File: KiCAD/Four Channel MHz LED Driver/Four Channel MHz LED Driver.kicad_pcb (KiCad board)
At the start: 2 copper layers, 100 x 100 mm, 92 parts, among them J1 Barrel_Jack_Switch, J10 Conn_01x24_Female, J2 Conn_01x02_Female, J3 8P8C_Shielded_x4, J4 Conn_01x03_Male, J5 Conn_01x03_Female, J6 Conn_01x08_Female, J7 Conn_01x03_Female, J8 Conn_01x05_Female, J9 Conn_01x24_Female, M1 Fan_4pin, Q1 SUM70060E, SW1 Pushbutton_with_LED, SW2 Pushbutton_with_LED, SW3 Pushbutton_with_LED, SW4 Pushbutton_with_LED, SW5 SW_SPDT, U1 12V boost, U10 ASSR-1218, U11 ASSR-1218, U12 Teensy3.6, U2 SN74LV4T125PWR, U3 DPBW06F-05, U4 TMUX1204DGSR, U5 BDJ0GA5WEFJ-E2, U6 ADP7182AUJZ-1.8-R7, U7 LT6200CS8-10, U8 ASSR-1218, U9 ASSR-1218

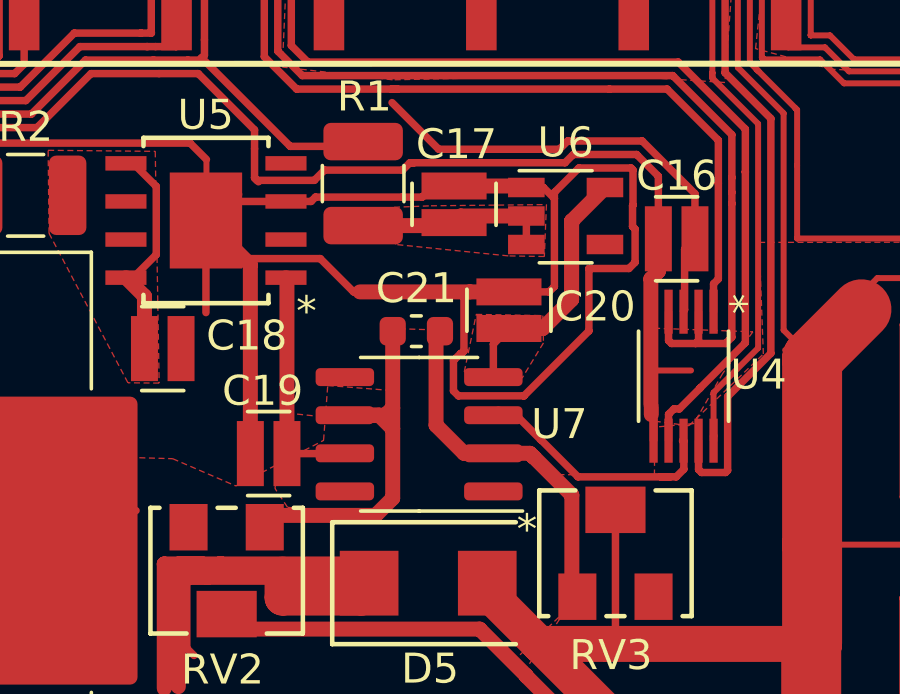
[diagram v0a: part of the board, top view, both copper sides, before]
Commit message: better LDO output bypass
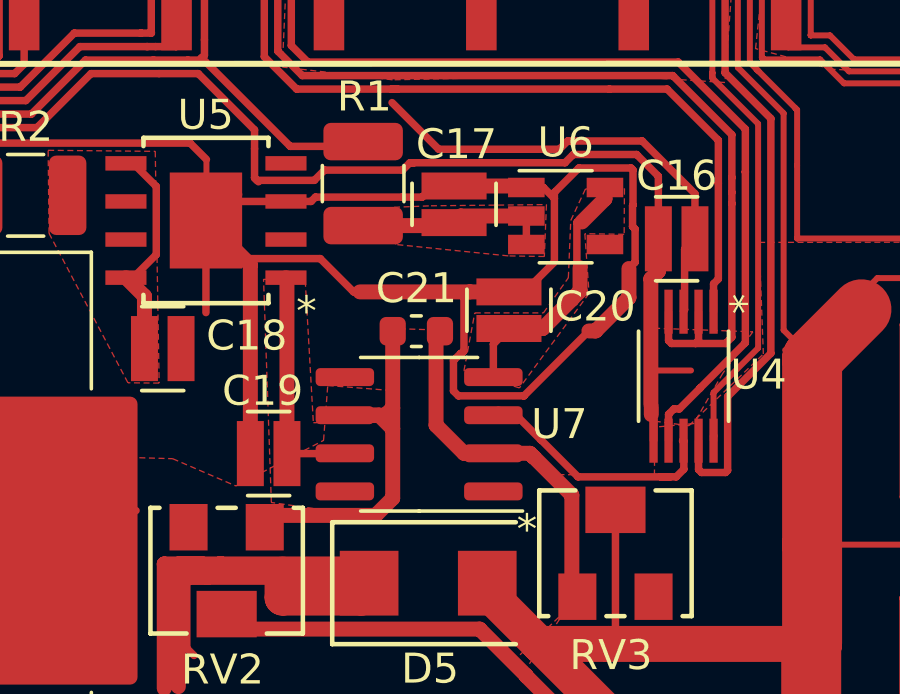
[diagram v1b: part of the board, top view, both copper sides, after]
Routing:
- net /-1.8V-analog: track 12.6 -> 8.70 mm
- net GND: track 1125.0 -> 1123.9 mm
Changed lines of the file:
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@@
     (thickness 1.6)
     (drawings 18)
-    (tracks 1936)
+    (tracks 1940)
     (zones 0)
     (modules 92)
@@
   (segment (start 59.11 58.57) (end 64.46 58.57) (width 0.25) (layer F.Cu) (net 2))
   (segment (start 82.77221 78.48) (end 78.81 78.48) (width 0.25) (layer F.Cu) (net 2))
-  (segment (start 96.885 71.19) (end 95.55 71.19) (width 0.25) (layer F.Cu) (net 2))
-  (segment (start 97.065001 71.009999) (end 96.885 71.19) (width 0.25) (layer F.Cu) (net 2))
-  (segment (start 97.065001 68.074999) (end 97.065001 71.009999) (width 0.25) (layer F.Cu) (net 2))
   (segment (start 96.700002 67.71) (end 97.065001 68.074999) (width 0.25) (layer F.Cu) (net 2))
   (segment (start 96.13 67.71) (end 96.700002 67.71) (width 0.25) (layer F.Cu) (net 2))
@@
   (segment (start 45.82 49.52) (end 46.66 50.36) (width 0.5) (layer F.Cu) (net 2))
   (segment (start 41.44 49.52) (end 45.82 49.52) (width 0.5) (layer F.Cu) (net 2))
-  (segment (start 98.215021 72.491747) (end 98.215021 70.41) (width 0.25) (layer F.Cu) (net 2))
   (segment (start 96.051758 74.65501) (end 98.215021 72.491747) (width 0.25) (layer F.Cu) (net 2))
   (segment (start 99.754999 69.094997) (end 99.67 69.009998) (width 0.25) (layer F.Cu) (net 2))
   (segment (start 99.754999 70.205001) (end 99.754999 69.094997) (width 0.25) (layer F.Cu) (net 2))
-  (segment (start 98.215021 70.41) (end 99.55 70.41) (width 0.25) (layer F.Cu) (net 2))
   (segment (start 99.55 70.41) (end 99.754999 70.205001) (width 0.25) (layer F.Cu) (net 2))
   (segment (start 62.27 103.77) (end 60.34 105.7) (width 2) (layer F.Cu) (net 2))
@@
   (segment (start 76.31998 66.23002) (end 84.92222 66.23002) (width 0.25) (layer F.Cu) (net 2))
   (segment (start 74.87 66.23002) (end 76.31998 66.23002) (width 0.25) (layer F.Cu) (net 2))
+  (segment (start 98.215021 72.491747) (end 98.438253 72.491747) (width 0.5) (layer F.Cu) (net 2))
+  (segment (start 99.55 71.38) (end 99.55 70.41) (width 0.5) (layer F.Cu) (net 2))
+  (segment (start 98.438253 72.491747) (end 99.55 71.38) (width 0.5) (layer F.Cu) (net 2))
+  (segment (start 96.070002 71.19) (end 95.55 71.19) (width 0.25) (layer F.Cu) (net 2))
+  (segment (start 97.065001 70.195001) (end 96.070002 71.19) (width 0.25) (layer F.Cu) (net 2))
+  (segment (start 97.065001 68.074999) (end 97.065001 70.195001) (width 0.25) (layer F.Cu) (net 2))
   (segment (start 45.34 54.5) (end 43.92 53.08) (width 0.25) (layer F.Cu) (net 3))
   (segment (start 45.34 56.08) (end 45.34 54.5) (width 0.25) (layer F.Cu) (net 3))
@@
   (segment (start 88.15 70.748) (end 88.117 70.715) (width 0.5) (layer F.Cu) (net 8))
   (segment (start 88.15 76.58) (end 88.15 70.748) (width 0.5) (layer F.Cu) (net 8))
-  (segment (start 98.75 67.71) (end 97.515011 68.944989) (width 0.25) (layer F.Cu) (net 9))
-  (segment (start 97.515011 68.944989) (end 97.51501 71.1964) (width 0.25) (layer F.Cu) (net 9))
   (segment (start 95.03 72.93) (end 95.55 72.41) (width 0.25) (layer F.Cu) (net 9))
   (segment (start 95.03 74.03) (end 95.03 72.93) (width 0.25) (layer F.Cu) (net 9))
-  (segment (start 97.640011 68.830011) (end 97.640011 68.944989) (width 0.5) (layer F.Cu) (net 9))
   (segment (start 98.75 67.71) (end 98.75 67.720022) (width 0.5) (layer F.Cu) (net 9))
-  (segment (start 98.75 67.720022) (end 97.640011 68.830011) (width 0.5) (layer F.Cu) (net 9))
-  (segment (start 97.640011 68.830011) (end 97.640011 71.248175) (width 0.5) (layer F.Cu) (net 9))
-  (segment (start 97.640011 71.444991) (end 97.640011 71.248175) (width 0.5) (layer F.Cu) (net 9))
   (segment (start 95.55 72.41) (end 96.675002 72.41) (width 0.5) (layer F.Cu) (net 9))
   (segment (start 96.675002 72.41) (end 97.640011 71.444991) (width 0.5) (layer F.Cu) (net 9))
+  (segment (start 98.75 67.71) (end 98.75 68.09) (width 0.5) (layer F.Cu) (net 9))
+  (segment (start 98.75 68.09) (end 97.98 68.86) (width 0.5) (layer F.Cu) (net 9))
+  (segment (start 97.640011 71.444991) (end 97.640011 71.439989) (width 0.5) (layer F.Cu) (net 9))
+  (segment (start 97.640011 71.439989) (end 97.92 71.16) (width 0.5) (layer F.Cu) (net 9))
+  (segment (start 97.92 71.16) (end 97.92 70.385001) (width 0.5) (layer F.Cu) (net 9))
+  (segment (start 97.814999 70.28) (end 97.92 70.385001) (width 0.25) (layer F.Cu) (net 9))
+  (segment (start 97.814999 68.875001) (end 97.814999 70.28) (width 0.25) (layer F.Cu) (net 9))
+  (segment (start 97.98 68.86) (end 97.83 68.86) (width 0.25) (layer F.Cu) (net 9))
+  (segment (start 97.83 68.86) (end 97.814999 68.875001) (width 0.25) (layer F.Cu) (net 9))
   (segment (start 97.771699 81.291699) (end 97.83 81.35) (width 0.25) (layer F.Cu) (net 82))
   (segment (start 93.12 75.635) (end 93.12 72.63) (width 0.5) (layer F.Cu) (net 82))
@@
     (polygon
       (pts
-        (xy 91.04 75.53) (xy 91.24 75.53) (xy 91.54 75.59) (xy 91.59 77.79) (xy 91.26 78.34)
-        (xy 90.29 78.59) (xy 88.17 78.37) (xy 87.75 77.74) (xy 88.17 75.23)
-      )
-    )
-  )
-  (zone (net 9) (net_name /-1.8V-analog) (layer F.Cu) (hatch edge 0.508)
-    (priority 4)
-    (connect_pads yes (clearance 0.21))
-    (min_thickness 0.254)
-    (fill yes (arc_segments 32) (thermal_gap 0.508) (thermal_bridge_width 0.508))
-    (polygon
-      (pts
-        (xy 96.68 71.98) (xy 96.7 72.89) (xy 95.99 74.06) (xy 94.06 73.86) (xy 94.46 71.94)
+        (xy 89.03 75.55) (xy 91.24 75.53) (xy 91.54 75.59) (xy 91.59 77.79) (xy 91.26 78.34)
+        (xy 90.29 78.59) (xy 87.63 78.21) (xy 87.37 70.77) (xy 88.76 70.82)
       )
     )
@@
       )
     )
+  )
+  (zone (net 9) (net_name /-1.8V-analog) (layer F.Cu) (hatch edge 0.508)
+    (priority 6)
+    (connect_pads yes (clearance 0.21))
+    (min_thickness 0.21)
+    (fill yes (arc_segments 32) (thermal_gap 0.508) (thermal_bridge_width 0.508))
+    (polygon
+      (pts
+        (xy 99.39 69.27) (xy 98.08 69.25) (xy 98.22 71.24) (xy 95.9 74.39) (xy 94.05 73.82)
+        (xy 94.41 71.89) (xy 96.7 71.89) (xy 97.53 70.72) (xy 97.61 68.81) (xy 98.1 67.76)
+        (xy 99.4 67.75)
+      )
+    )

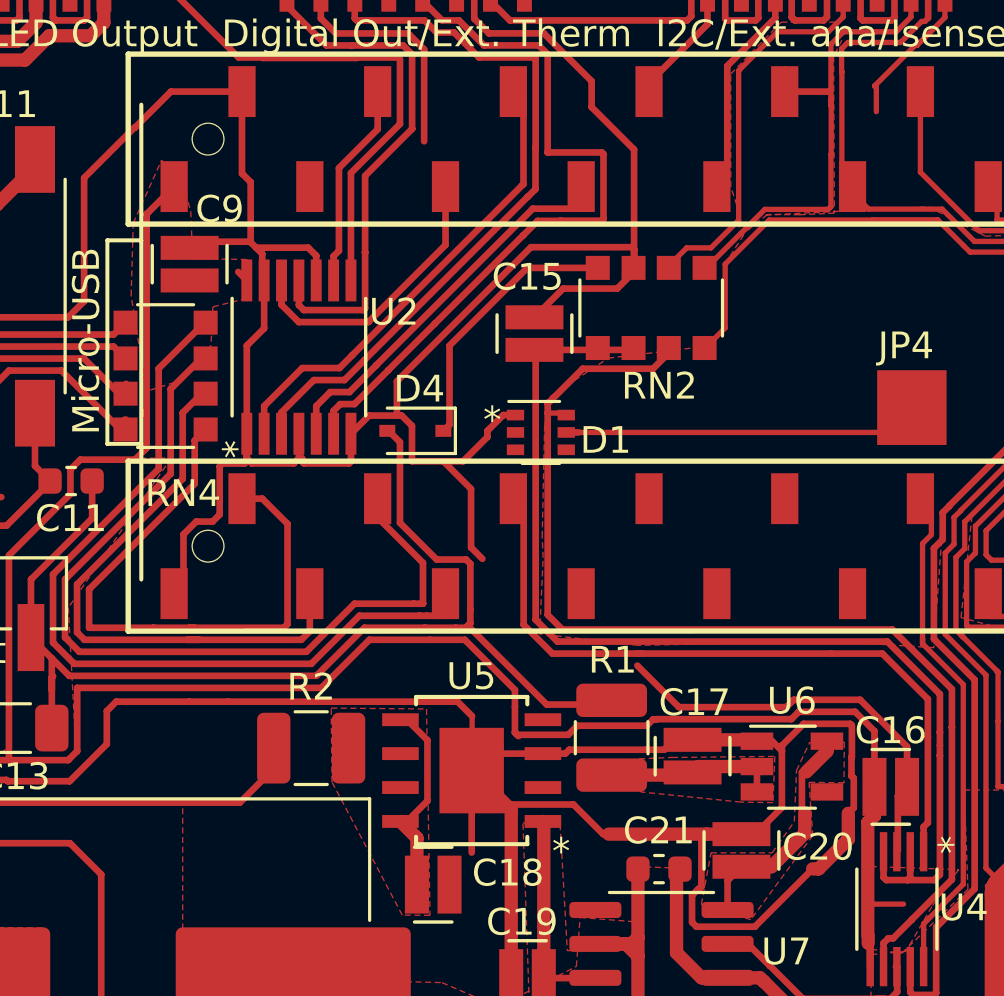
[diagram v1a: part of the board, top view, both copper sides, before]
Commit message: bypass pour optimization
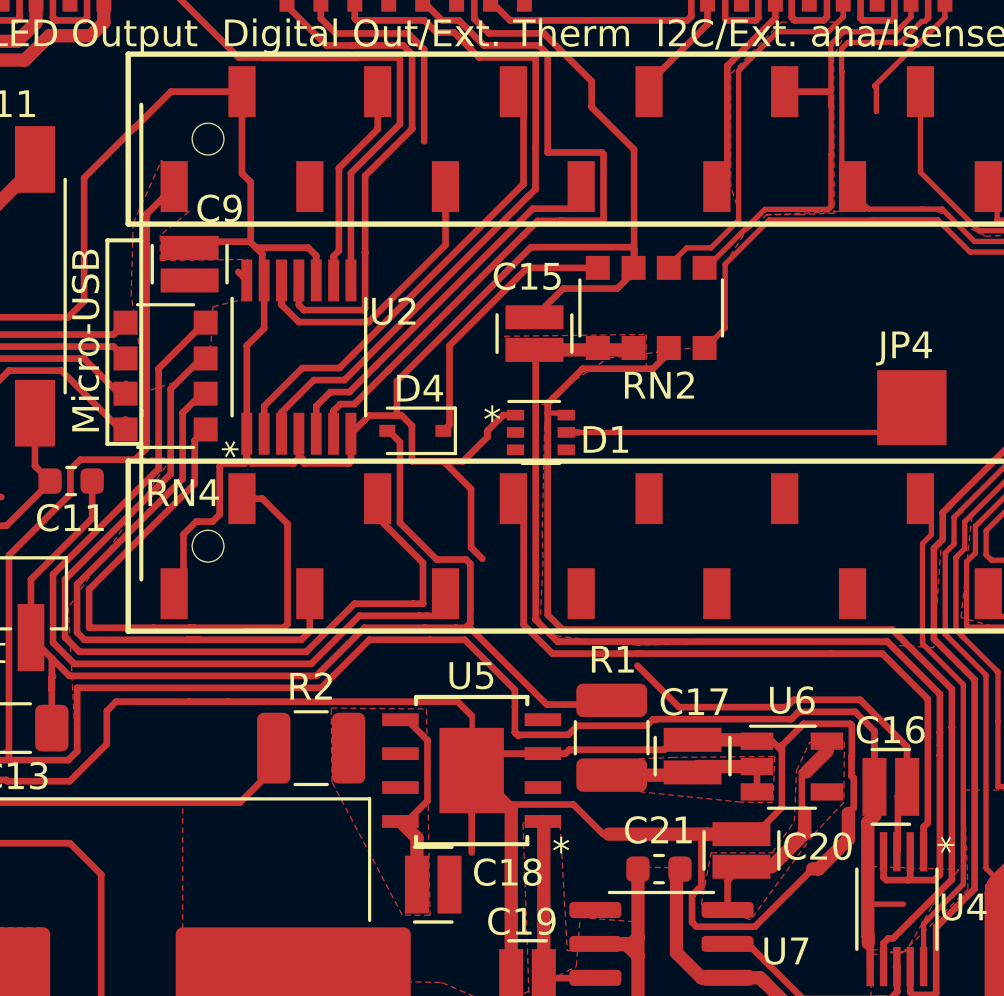
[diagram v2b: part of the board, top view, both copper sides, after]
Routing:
- net /-0.25V_analog: track 41.2 -> 45.0 mm
- added copper zone on F.Cu, net /-0.25V_analog
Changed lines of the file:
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@@
     (thickness 1.6)
     (drawings 18)
-    (tracks 1940)
+    (tracks 1942)
     (zones 0)
     (modules 92)
@@
   )
   (setup
-    (last_trace_width 0.25)
+    (last_trace_width 1.2)
     (user_trace_width 0.2)
     (user_trace_width 0.5)
@@
   (segment (start 102.98 67.874114) (end 102.98 67.37637) (width 0.25) (layer F.Cu) (net 6))
   (segment (start 102.97999 67.37636) (end 102.97999 65.94999) (width 0.25) (layer F.Cu) (net 6))
+  (segment (start 91.44 53.06) (end 91.51 52.99) (width 0.5) (layer F.Cu) (net 6))
+  (segment (start 87.8 53.06) (end 91.44 53.06) (width 0.5) (layer F.Cu) (net 6))
   (segment (start 90.69 68.98) (end 93.3 68.98) (width 0.25) (layer F.Cu) (net 7))
   (segment (start 96.13 69.61) (end 96.13 68.66) (width 0.25) (layer F.Cu) (net 7))
@@
     (polygon
       (pts
-        (xy 74.64 46.83) (xy 74.93 47.87) (xy 75.005 49.645) (xy 77.055 49.675) (xy 77.03 51.13)
+        (xy 74.87 47.88) (xy 73.79 48.77) (xy 73.79 49.71) (xy 77.055 49.675) (xy 77.03 51.13)
         (xy 75.76 51.45) (xy 75.69 52.9) (xy 74.32 54.28) (xy 73.27 54.61) (xy 72.7 51.03)
         (xy 72.78 48.31) (xy 73.84 45.96)
@@
     (polygon
       (pts
-        (xy 99.39 69.27) (xy 98.08 69.25) (xy 98.22 71.24) (xy 95.9 74.39) (xy 94.05 73.82)
+        (xy 99.39 69.27) (xy 99.39 69.99) (xy 98.22 71.24) (xy 95.9 74.39) (xy 94.05 73.82)
         (xy 94.41 71.89) (xy 96.7 71.89) (xy 97.53 70.72) (xy 97.61 68.81) (xy 98.1 67.76)
         (xy 99.4 67.75)
       )
     )
+  )
+  (zone (net 6) (net_name /-0.25V_analog) (layer F.Cu) (hatch edge 0.508)
+    (priority 8)
+    (connect_pads yes (clearance 0.21))
+    (min_thickness 0.21)
+    (fill yes (arc_segments 32) (thermal_gap 0.508) (thermal_bridge_width 0.508))
+    (polygon
+      (pts
+        (xy 91.99 53.76) (xy 89.64 53.75) (xy 88.28 55.15) (xy 87.9 55.02) (xy 87.86 53.48)
+        (xy 86.67 52.55) (xy 91.98 52.48)
+      )
+    )

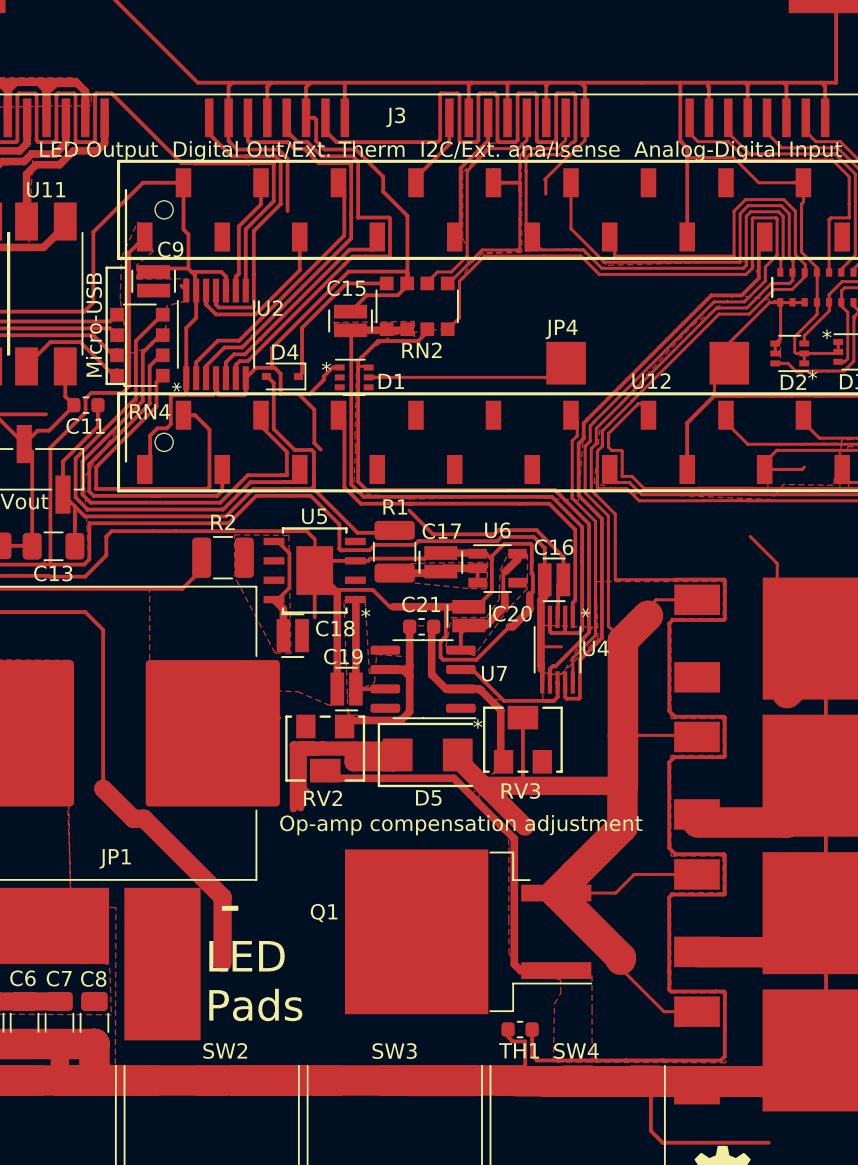
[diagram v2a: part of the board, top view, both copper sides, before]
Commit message: Fixed error of disconnected FB pin on 10V LDO and improved cap placement
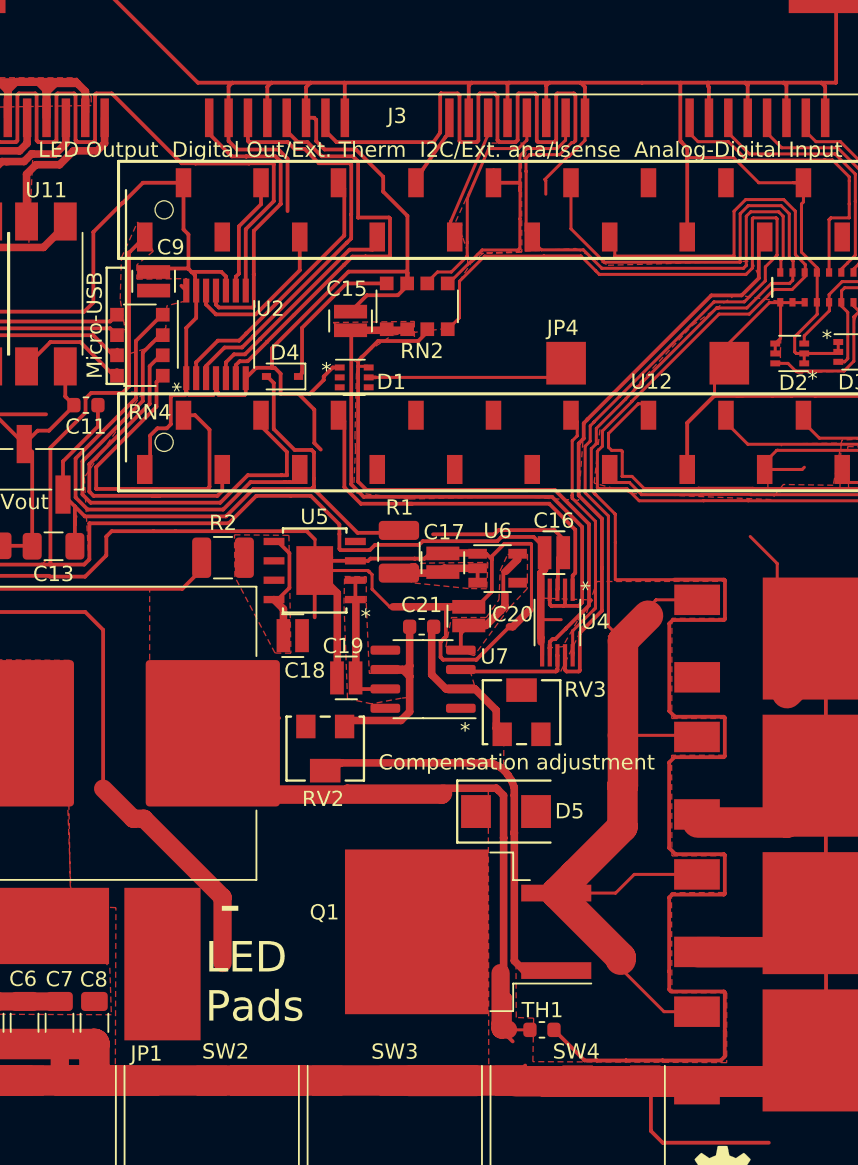
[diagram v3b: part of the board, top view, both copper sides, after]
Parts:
- moved D5 6.33 mm to (98.0, 84.6)
- moved RV3 1.81 mm to (99.0, 78.1)
- moved C16 1.78 mm to (101.1, 67.6)
- moved U4 1.78 mm to (101.4, 72.2)
- moved TH1 1.44 mm to (100.3, 98.9)
- moved C19 0.73 mm to (87.5, 75.8)
- moved R1 0.28 mm to (91.0, 67.6)
- moved C17 0.13 mm to (93.8, 68.3)
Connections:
- U5 pad 2: Net-(U5-Pad2) -> /10V-analog
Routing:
- net GND: track 1123.9 -> 1178.7 mm
- net /LED-: track 169.4 -> 139.5 mm
- net /Isense: track 138.0 -> 117.8 mm
- net Net-(Q1-Pad1): track 25.3 -> 29.1 mm
- net /MOSFET_temp: track 127.9 -> 125.4 mm
- net Net-(C21-Pad2): track 12.2 -> 10.1 mm
- net /5V: track 102.4 -> 100.4 mm
- net /Interline_PWM: track 27.1 -> 25.4 mm
- net /external_analog: track 42.0 -> 40.2 mm
- net /-0.25V_analog: track 45.0 -> 43.2 mm
- net /internal_analog: track 39.6 -> 37.9 mm
- net /Analog_select: track 19.5 -> 17.9 mm
- net /10V-analog: track 7.81 -> 9.08 mm
- net /SDA0: track 11.0 -> 11.9 mm
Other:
- board text added: "Compensation adjustment"
- board text removed: "Op-amp compensation adjustment"
